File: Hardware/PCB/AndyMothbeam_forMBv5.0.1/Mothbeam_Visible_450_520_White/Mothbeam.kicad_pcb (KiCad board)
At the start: 2 copper layers, 27.8 x 45 mm, 23 parts, among them CN1 X6511FRS-04-C85D30, SW2 SW_DIP_x04, U1 BCR421U, U2 BCR421U, U3 BCR421U

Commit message: before changing footprints on Visible board
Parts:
- removed D1: LED1, easyeda2kicad:LED-SMD_3P-L3.5-W3.5-R-RD-C
- removed D2: LED2, easyeda2kicad:LED-SMD_3P-L3.5-W3.5-R-RD-C
- removed D3: LED3, easyeda2kicad:LED-SMD_3P-L3.5-W3.5-R-RD-C
- removed REF** (x2): MountingHole_2.2mm_M2_DIN965_Pad, MountingHole:MountingHole_2.2mm_M2_DIN965_Pad
- added LED2: JNJ-LEJB0111W60/26MIL/450-460NM, easyeda2kicad:LED-SMD_3P-L3.5-W3.5_JNJ-LEJB0111W60, F.Cu at (112.8, 37.8)
- added LED3: JNJ-LEJW0113W30/C36MIL/5500-6500K, easyeda2kicad:LED-SMD_3P-L3.5-W3.5-R-RD-B, F.Cu at (112.8, 54.0)
- added U6: JNJ-LEHG0113W120/45MIL/525-530NM, easyeda2kicad:LED-SMD_3P-L3.5-W3.5-R-RD_C9900043159, F.Cu at (112.7, 45.9)

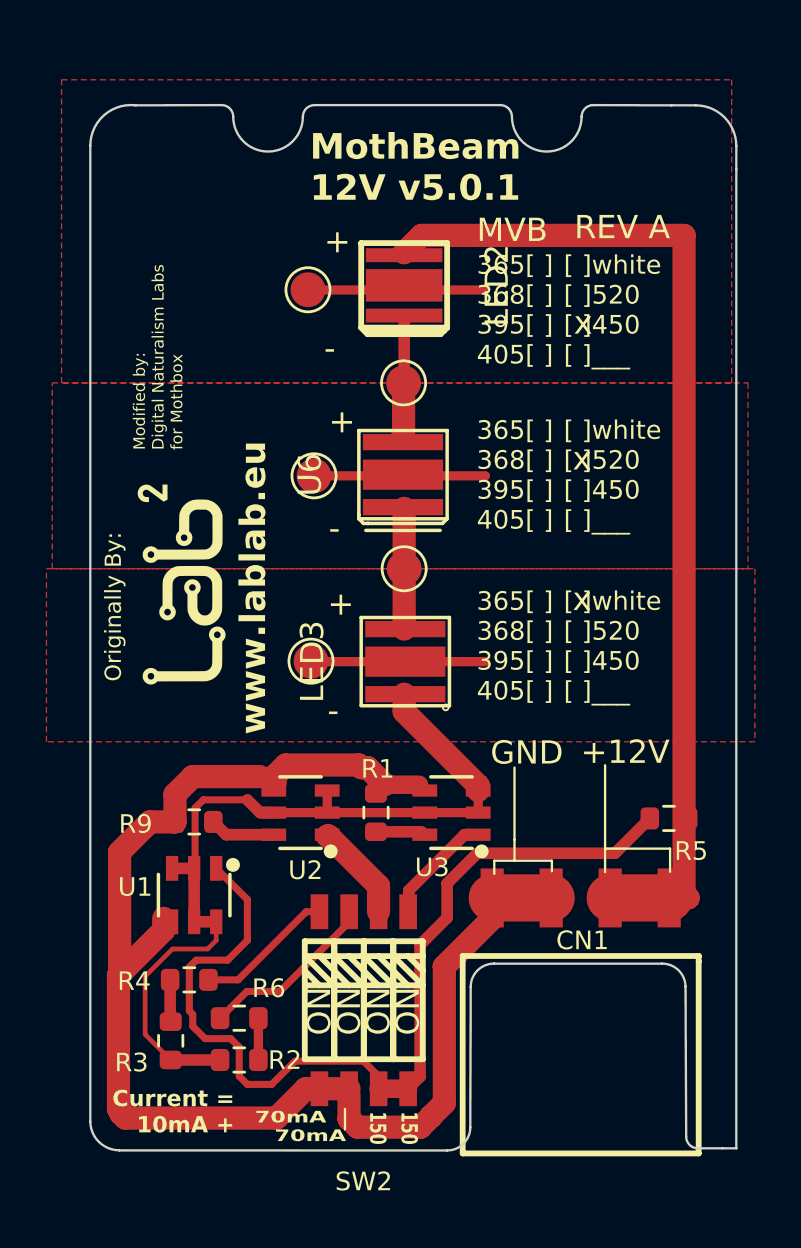
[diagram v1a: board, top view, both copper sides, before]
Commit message: new substitute parts
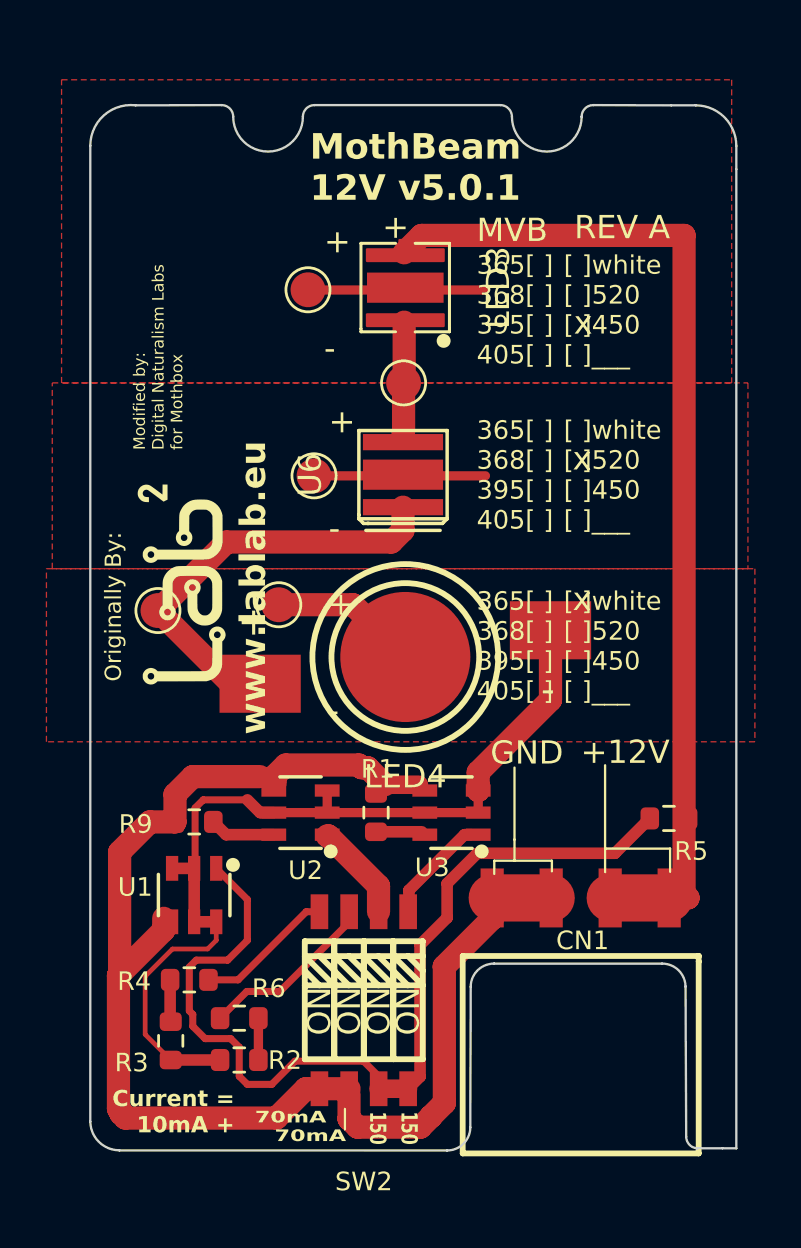
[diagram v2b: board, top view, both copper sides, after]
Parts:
- removed LED2: JNJ-LEJB0111W60/26MIL/450-460NM, easyeda2kicad:LED-SMD_3P-L3.5-W3.5_JNJ-LEJB0111W60
- added LED4: XL-HD6070UWC-A2-BD, easyeda2kicad:LED-SMD_XL-HD6070UBC-A2, F.Cu at (112.8, 53.8)
- LED3: value JNJ-LEJW0113W30/C36MIL/5500-6500K -> JNJ-LTJB0115W30/56MIL/450-460NM; footprint easyeda2kicad:LED-SMD_3P-L3.5-W3.5-R-RD-B -> easyeda2kicad:LED-SMD_3P-L3.5-W3.5-FD-1
- moved LED3 16.1 mm to (112.8, 37.9), turned to -90 degrees
- moved TP1 10.8 mm to (102.2, 51.8)
- moved TP5 2.80 mm to (107.3, 51.5)
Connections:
- LED3 pad 1: Net-(U6-K) -> /LED+
- LED3 pad 2: /T3 -> Net-(LED3-K)
- LED3 pad 3: /LED- -> /T1
- TP1 pad 1: Net-(U6-K) -> Net-(LED4-A)
- TP3 pad 1: Net-(LED2-K-Pad1) -> Net-(LED3-K)
- U6 pad 1: Net-(LED2-K-Pad1) -> Net-(LED3-K)
- U6 pad 3: Net-(U6-K) -> Net-(LED4-A)
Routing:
- net Net-(LED4-A): track 0.00 -> 18.7 mm
- net Net-(U6-K): track 5.36 -> 0.00 mm
- net Net-(LED3-K): track 0.00 -> 4.75 mm
- net Net-(LED2-K-Pad1): track 4.75 -> 0.00 mm
- net /LED-: track 37.4 -> 40.3 mm
- net /T3: track 7.00 -> 6.38 mm

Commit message: Created 3535 Mothbeams for UV and V
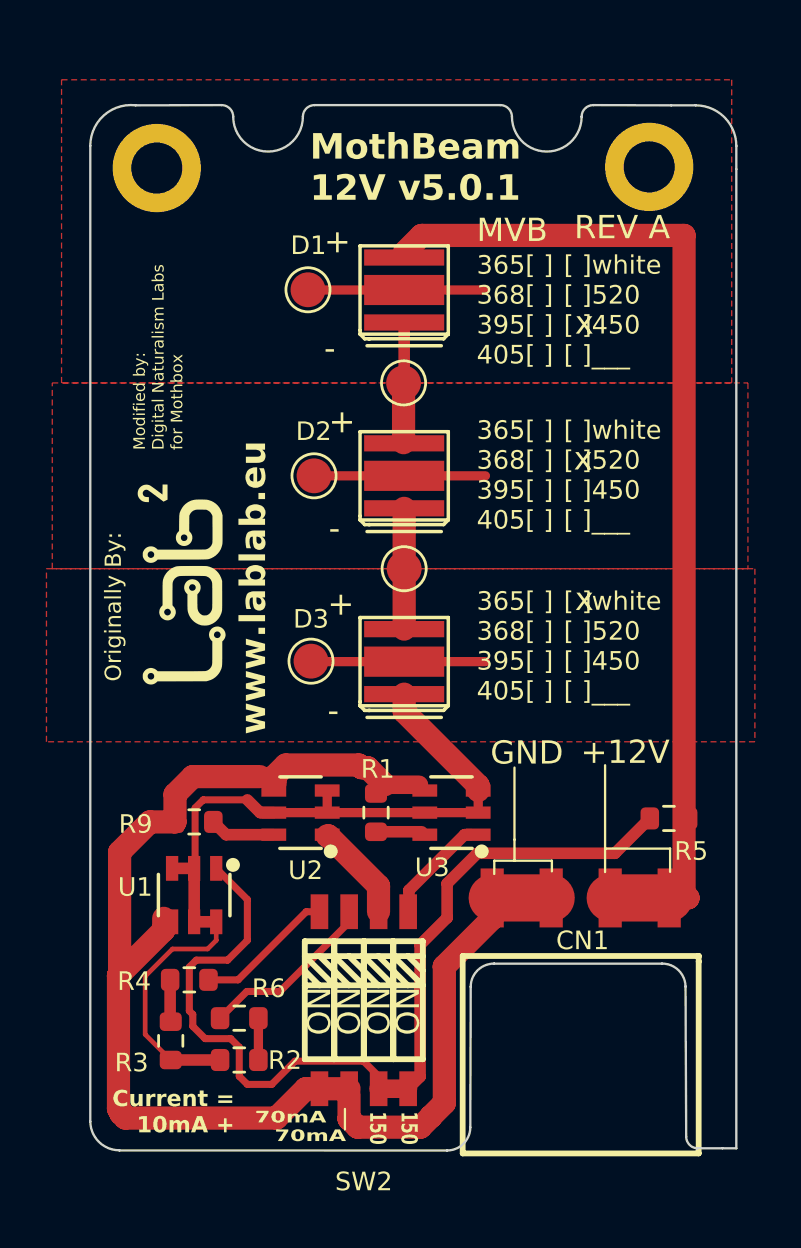
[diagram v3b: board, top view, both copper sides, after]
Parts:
- removed LED3: JNJ-LTJB0115W30/56MIL/450-460NM, easyeda2kicad:LED-SMD_3P-L3.5-W3.5-FD-1
- removed LED4: XL-HD6070UWC-A2-BD, easyeda2kicad:LED-SMD_XL-HD6070UBC-A2
- removed U6: JNJ-LEHG0113W120/45MIL/525-530NM, easyeda2kicad:LED-SMD_3P-L3.5-W3.5-R-RD_C9900043159
- added D1: LED1, easyeda2kicad:LED-SMD_3P-L3.5-W3.5-R-RD-C, F.Cu at (112.8, 38.0)
- added D2: LED2, easyeda2kicad:LED-SMD_3P-L3.5-W3.5-R-RD-C, F.Cu at (112.8, 46.0)
- added D3: LED3, easyeda2kicad:LED-SMD_3P-L3.5-W3.5-R-RD-C, F.Cu at (112.8, 54.0)
- added REF**: MountingHole_2.2mm_M2_DIN965_Pad, MountingHole:MountingHole_2.2mm_M2_DIN965_Pad, F.Cu at (102.1, 32.7)
- added REF**: MountingHole_2.2mm_M2_DIN965_Pad, MountingHole:MountingHole_2.2mm_M2_DIN965_Pad, F.Cu at (123.3, 32.6)
- moved TP1 10.8 mm to (112.8, 50.0)
- moved TP5 2.80 mm to (108.7, 53.9)
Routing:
- net Net-(D2-A): track 18.7 -> 5.36 mm
- net /LED-: track 40.3 -> 37.4 mm
- net /T3: track 6.38 -> 7.00 mm

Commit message: Updated Visible PCB for JLCPCB order
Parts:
- REF** (x2): value MountingHole_2.2mm_M2_DIN965_Pad -> MountingHole_3.2mm_M3; footprint MountingHole:MountingHole_2.2mm_M2_DIN965_Pad -> MountingHole:MountingHole_3.2mm_M3
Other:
- board text added: "MothBeam 12V v5.0.2"
- board text added: "Visible"
- board text removed: "MVB"
- board text removed: "MothBeam 12V v5.0.1"
- board text removed: "REV A"
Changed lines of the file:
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@@
 	)
 	(paper "A4")
+	(title_block
+		(title "Mothbeam Visible")
+		(company "Digital Naturalism Laboratories")
+	)
 	(layers
 		(0 "F.Cu" signal)
@@
 	(net 16 "Net-(D1--)")
 	(net 17 "Net-(D2-A)")
-	(footprint "MountingHole:MountingHole_2.2mm_M2_DIN965_Pad"
+	(footprint "MountingHole:MountingHole_3.2mm_M3"
 		(layer "F.Cu")
 		(at 102.1 32.7)
-		(descr "Mounting Hole 2.2mm, M2, generated by kicad-footprint-generator mountinghole.py")
-		(tags "mountinghole M2 DIN965")
+		(descr "Mounting Hole 3.2mm, M3, no annular, generated by kicad-footprint-generator mountinghole.py")
+		(tags "mountinghole M3")
 		(property "Reference" "REF**"
-			(at 0 -2.85 0)
+			(at 0 -4.15 0)
 			(layer "F.SilkS")
-			(hide yes)
 			(effects
 				(font
-					(size 0.8 0.8)
+					(size 1 1)
 					(thickness 0.15)
 				)
 			)
 		)
-		(property "Value" "MountingHole_2.2mm_M2_DIN965_Pad"
-			(at 0 2.85 0)
+		(property "Value" "MountingHole_3.2mm_M3"
+			(at 0 4.15 0)
 			(layer "F.Fab")
 			(effects
@@
 		(fp_circle
 			(center 0 0)
-			(end 1.9 0)
+			(end 3.2 0)
 			(stroke
 				(width 0.15)
@@
 		(fp_circle
 			(center 0 0)
-			(end 2.15 0)
+			(end 3.45 0)
 			(stroke
 				(width 0.05)
@@
 			(effects
 				(font
-					(size 0.95 0.95)
-					(thickness 0.14)
+					(size 1 1)
+					(thickness 0.15)
 				)
 			)
 		)
-		(pad "1" thru_hole circle
+		(pad "" np_thru_hole circle
 			(at 0 0)
-			(size 3.8 3.8)
-			(drill 2.2)
+			(size 3.2 3.2)
+			(drill 3.2)
 			(layers "*.Cu" "*.Mask")
-			(remove_unused_layers no)
-			(zone_connect 2)
 		)
 		(embedded_fonts no)
@@
 		)
 	)
-	(footprint "MountingHole:MountingHole_2.2mm_M2_DIN965_Pad"
+	(footprint "MountingHole:MountingHole_3.2mm_M3"
 		(layer "F.Cu")
 		(at 123.3 32.65)
-		(descr "Mounting Hole 2.2mm, M2, generated by kicad-footprint-generator mountinghole.py")
-		(tags "mountinghole M2 DIN965")
+		(descr "Mounting Hole 3.2mm, M3, no annular, generated by kicad-footprint-generator mountinghole.py")
+		(tags "mountinghole M3")
 		(property "Reference" "REF**"
-			(at 0 -2.85 0)
+			(at 0 -4.15 0)
 			(layer "F.SilkS")
-			(hide yes)
 			(effects
 				(font
-					(size 0.8 0.8)
+					(size 1 1)
 					(thickness 0.15)
 				)
 			)
 		)
-		(property "Value" "MountingHole_2.2mm_M2_DIN965_Pad"
-			(at 0 2.85 0)
+		(property "Value" "MountingHole_3.2mm_M3"
+			(at 0 4.15 0)
 			(layer "F.Fab")
 			(effects
@@
 		(fp_circle
 			(center 0 0)
-			(end 1.9 0)
+			(end 3.2 0)
 			(stroke
 				(width 0.15)
@@
 		(fp_circle
 			(center 0 0)
-			(end 2.15 0)
+			(end 3.45 0)
 			(stroke
 				(width 0.05)
@@
 			(effects
 				(font
-					(size 0.95 0.95)
-					(thickness 0.14)
+					(size 1 1)
+					(thickness 0.15)
 				)
 			)
 		)
-		(pad "1" thru_hole circle
+		(pad "" np_thru_hole circle
 			(at 0 0)
-			(size 3.8 3.8)
-			(drill 2.2)
+			(size 3.2 3.2)
+			(drill 3.2)
 			(layers "*.Cu" "*.Mask")
-			(remove_unused_layers no)
-			(zone_connect 2)
 		)
 		(embedded_fonts no)
@@
 		)
 	)
-	(gr_text "REV A"
-		(at 120.07 35.84 0)
-		(layer "F.SilkS")
-		(effects
-			(font
-				(size 1 1)
-				(thickness 0.15)
-			)
-			(justify left bottom)
-		)
-	)
 	(gr_text "x"
 		(at 120.1 51.85 0)
@@
 		)
 	)
-	(gr_text "MothBeam\n12V v5.0.1"
+	(gr_text "MothBeam\n12V v5.0.2\n"
 		(at 108.69 34.2 0)
 		(layer "F.SilkS" knockout)
@@
 			(justify left bottom)
 		)
-		(render_cache "MothBeam\n12V v5.0.1" 0
+		(render_cache "MothBeam\n12V v5.0.2\n" 0
 			(polygon
 				(pts
@@
 			(polygon
 				(pts
-					(xy 115.999693 34.013) (xy 115.767162 34.013) (xy 115.767162 33.376997) (xy 115.768707 33.27309)
-					(xy 115.773341 33.158302) (xy 115.740228 33.191415) (xy 115.693278 33.23373) (xy 115.566938 33.335421)
-					(xy 115.454568 33.195244) (xy 115.808738 32.913412) (xy 115.999693 32.913412)
+					(xy 116.193738 34.013) (xy 115.425283 34.013) (xy 115.425283 33.851329) (xy 115.700935 33.572587)
+					(xy 115.834933 33.428581) (xy 115.880699 33.370849) (xy 115.908817 33.323868) (xy 115.926106 33.27531)
+					(xy 115.931922 33.222984) (xy 115.927386 33.180351) (xy 115.915048 33.148366) (xy 115.895719 33.12445)
+					(xy 115.86987 33.106988) (xy 115.837855 33.096013) (xy 115.797991 33.092076) (xy 115.736043 33.099294)
+					(xy 115.67474 33.12136) (xy 115.615191 33.155418) (xy 115.548467 33.204513) (xy 115.422193 33.055134)
+					(xy 115.522272 32.9789) (xy 115.579286 32.946623) (xy 115.646262 32.920397) (xy 115.720273 32.904058)
+					(xy 115.814918 32.898031) (xy 115.885918 32.902734) (xy 115.947282 32.916089) (xy 116.000499 32.937323)
+					(xy 116.049213 32.967155) (xy 116.088909 33.002481) (xy 116.120594 33.043581) (xy 116.143986 33.089802)
+					(xy 116.158135 33.14002) (xy 116.162976 33.195244) (xy 116.15883 33.254988) (xy 116.146699 33.310199)
+					(xy 116.126773 33.361616) (xy 116.083716 33.434901) (xy 116.021993 33.510995) (xy 115.949161 33.585977)
+					(xy 115.856494 33.67421) (xy 115.714839 33.806663) (xy 115.714839 33.81741) (xy 116.193738 33.81741)
 				)
 			)
 		)
 	)
-	(gr_text "MVB"
+	(gr_text "Visible"
 		(at 115.87 35.96 0)
 		(layer "F.SilkS")
@@
 	)
 	(zone
-		(net 9)
-		(net_name "/T2")
-		(layer "F.Cu")
-		(hatch edge 0.5)
-		(connect_pads
-			(clearance 0.35)
-		)
-		(min_thickness 0.25)
-		(filled_areas_thickness no)
-		(fill yes
-			(thermal_gap 0.5)
-			(thermal_bridge_width 0.5)
-			(smoothing chamfer)
-		)
-		(polygon
-			(pts
-				(xy 127.55 41.95) (xy 127.55 49.95) (xy 97.6 49.95) (xy 97.6 41.95)
-			)
-		)
-	)
-	(zone
 		(net 17)
 		(net_name "Net-(D2-A)")
@@
 			)
 		)
+	)
+	(zone
+		(net 9)
+		(net_name "/T2")
+		(layer "F.Cu")
+		(hatch edge 0.5)
+		(connect_pads
+			(clearance 0.35)
+		)
+		(min_thickness 0.25)
+		(filled_areas_thickness no)
+		(fill yes
+			(thermal_gap 0.5)
+			(thermal_bridge_width 0.5)
+			(smoothing chamfer)
+		)
+		(polygon
+			(pts
+				(xy 127.55 41.95) (xy 127.55 49.95) (xy 97.6 49.95) (xy 97.6 41.95)
+			)
+		)
